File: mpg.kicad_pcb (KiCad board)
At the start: 2 copper layers, 57 parts, among them J1 Conn_01x04_Male, J2 DB25_Male_MountingHoles, J3 Conn_01x03_Male, J4 Screw_Terminal_01x02, J5 Screw_Terminal_01x03, J6 Screw_Terminal_01x03, K1 G5LE-1, Q1 BC847, Q2 BC847, Q3 BC847, Q4 BC847, Q5 BC847, SW1 SW_Push, U1 LD2981ABU33TR, U2 SP3485CN

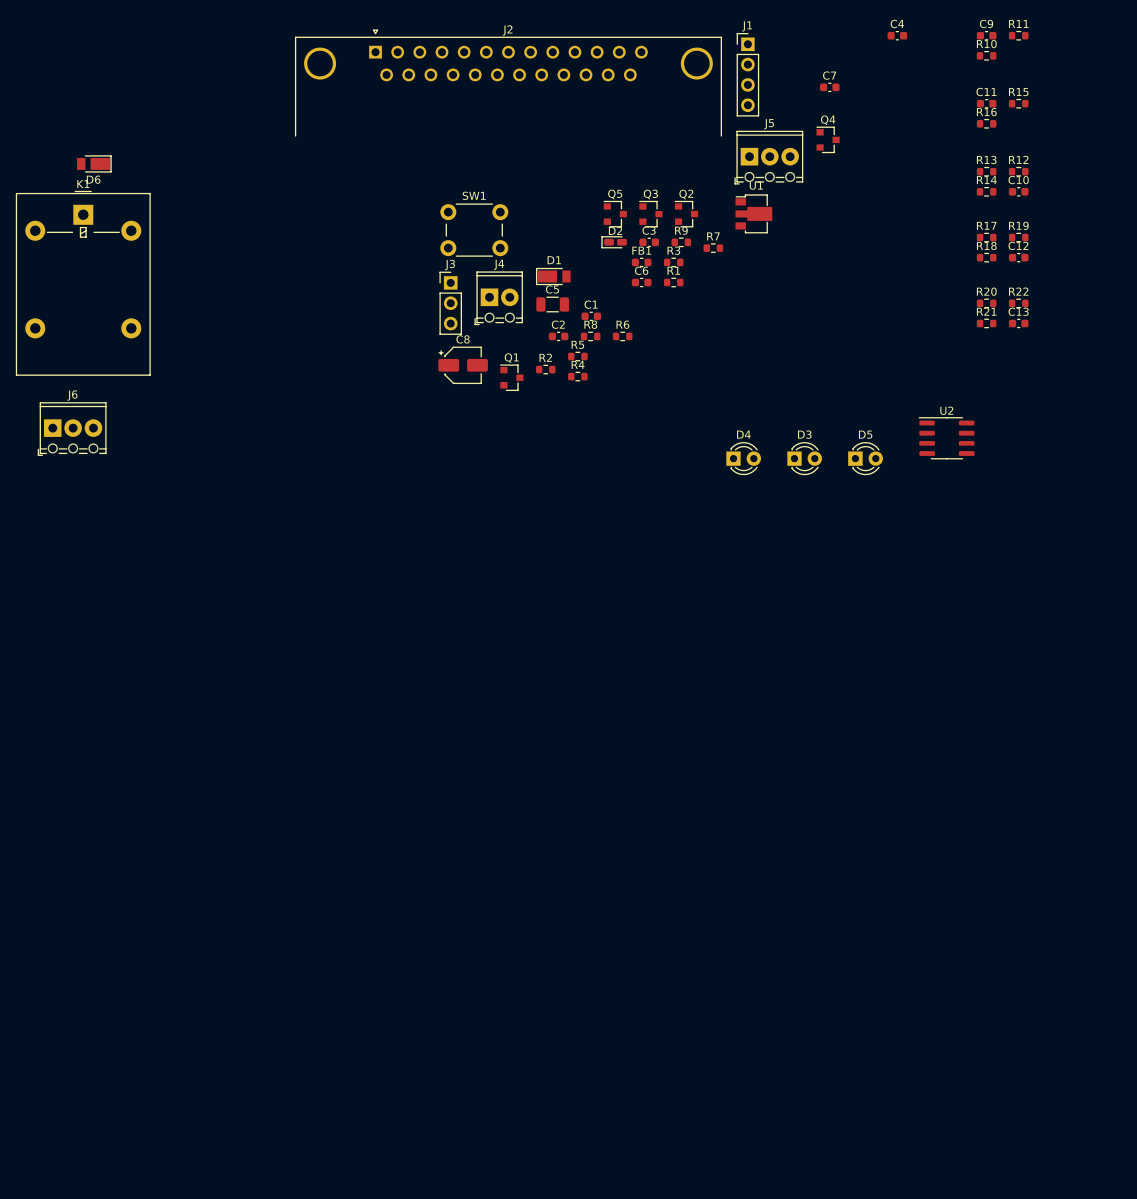
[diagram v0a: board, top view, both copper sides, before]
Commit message: Corrected STM32 symbol and generated PCB.
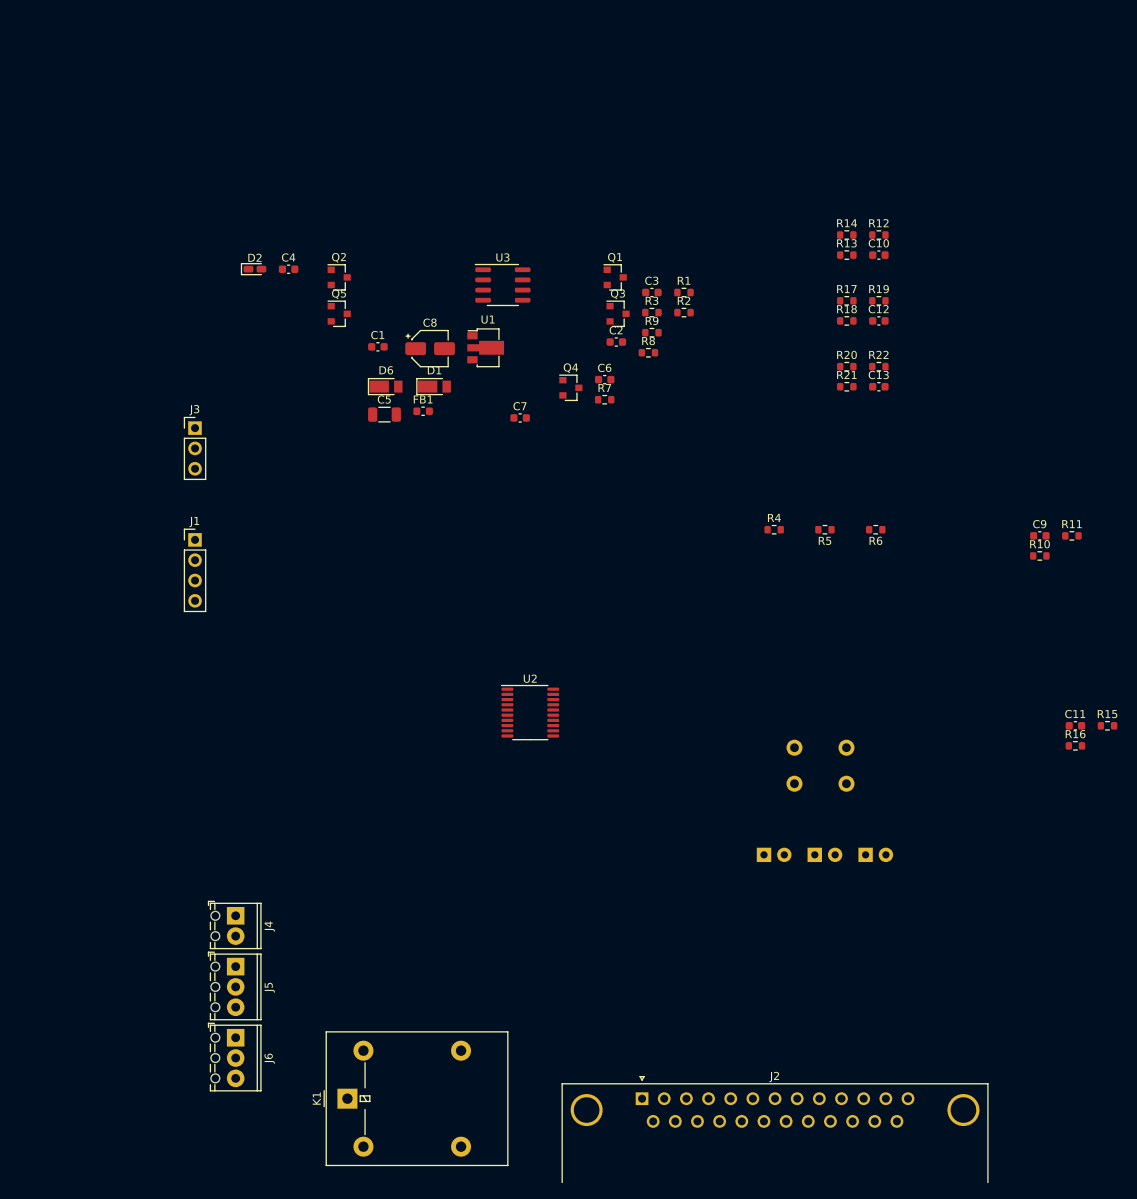
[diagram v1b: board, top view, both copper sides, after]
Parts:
- added U3: SP3485CN, Package_SO:SOIC-8_3.9x4.9mm_P1.27mm, F.Cu at (109.6, 54.5)
- D3, D4, D5, SW1: moved to B.Cu
- U2: value SP3485CN -> STM32G031F4Px; footprint Package_SO:SOIC-8_3.9x4.9mm_P1.27mm -> Package_SO:TSSOP-20_4.4x6.5mm_P0.65mm
- moved J2 135.0 mm to (127.0, 156.2)
- moved J5 119.9 mm to (76.2, 139.7), turned to 270 degrees
- moved K1 115.3 mm to (90.2, 156.2), turned to 90 degrees
- moved J1 92.8 mm to (71.1, 86.4)
- moved J4 83.6 mm to (76.2, 133.3), turned to 270 degrees
- moved SW1 83.5 mm to (146.1, 116.8)
- moved C4 81.5 mm to (82.8, 52.5)
- moved J6 79.6 mm to (76.2, 148.6), turned to 270 degrees
- moved C11 78.5 mm to (181.2, 109.6)
- moved R15 78.5 mm to (185.2, 109.6)
- moved R16 78.5 mm to (181.2, 112.1)
- moved R10 62.9 mm to (176.7, 88.4)
- moved C9 62.9 mm to (176.7, 85.9)
- moved R11 62.9 mm to (180.7, 85.9)
- moved U2 62.3 mm to (113.0, 108.0)
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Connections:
- U2 pad 2: USART1_RTS -> LED_A
- U2 pad 3: USART1_RTS -> LED_B
- U2 pad 4: USART1_TX -> +3V3
- U2 pad 6: Net-(J5-Pad2) -> RESET
- U2 pad 7: Net-(J5-Pad3) -> XYZ
- U2 pad 8: +3V3 -> LED_C

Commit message: Better layout.
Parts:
- moved C4 111.8 mm to (124.0, 156.5)
- moved R3 102.7 mm to (123.4, 160.5)
- moved J1 97.4 mm to (139.2, 156.0), turned to 270 degrees
- moved U3 93.7 mm to (117.9, 147.8), turned to 180 degrees
- moved R22 90.3 mm to (153.4, 154.9)
- moved C13 88.0 mm to (149.4, 154.9)
- moved R2 87.3 mm to (87.9, 133.1)
- moved R20 86.7 mm to (149.4, 151.4)
- moved Q5 85.7 mm to (105.7, 142.2)
- moved Q1 85.4 mm to (153.4, 133.6)
- moved R8 85.4 mm to (111.8, 146.8), turned to 90 degrees
- moved D2 84.8 mm to (87.8, 136.8)
- moved R21 84.2 mm to (153.4, 151.4), turned to 180 degrees
- moved R9 83.7 mm to (110.2, 142.2), turned to 180 degrees
- moved R1 79.0 mm to (149.4, 132.6), turned to 180 degrees
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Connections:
- J2 pad 10: /sheet603130A5/S2 -> XYZ
- J2 pad 11: /sheet603130A5/S3 -> /sheet603130A5/S2
- J2 pad 12: ABC -> /Sheet602C38D3/S2
- J2 pad 13: /Sheet602C38D3/S2 -> ABC
- J2 pad 9: XYZ -> /sheet603130A5/S3
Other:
- board outline added: 97.5 x 59.4 mm

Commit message: Smaller is better!
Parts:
- moved D6 47.6 mm to (138.2, 160.5)
- moved J3 45.2 mm to (153.9, 111.8), turned to 270 degrees
- moved D1 42.4 mm to (112.8, 112.3)
- moved J4 39.8 mm to (110.7, 121.9)
- moved C1 39.7 mm to (134.1, 131.6), turned to 90 degrees
- moved J6 36.3 mm to (110.7, 137.4)
- moved J5 34.8 mm to (110.7, 128.5)
- moved FB1 32.0 mm to (121.4, 121.4), turned to 90 degrees
- moved R7 31.6 mm to (133.1, 144.8), turned to 0 degrees
- moved SW1 31.5 mm to (143.8, 155.4), turned to 90 degrees
- moved D2 30.9 mm to (118.5, 133.4), turned to 180 degrees
- moved R2 30.7 mm to (118.4, 137.2)
- moved C5 29.5 mm to (117.9, 121.4), turned to 180 degrees
- moved K1 29.5 mm to (131.6, 155.4)
- moved C3 29.3 mm to (123.4, 131.6), turned to 90 degrees
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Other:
- board size 97.5 x 59.4 mm -> 63.5 x 59.4 mm

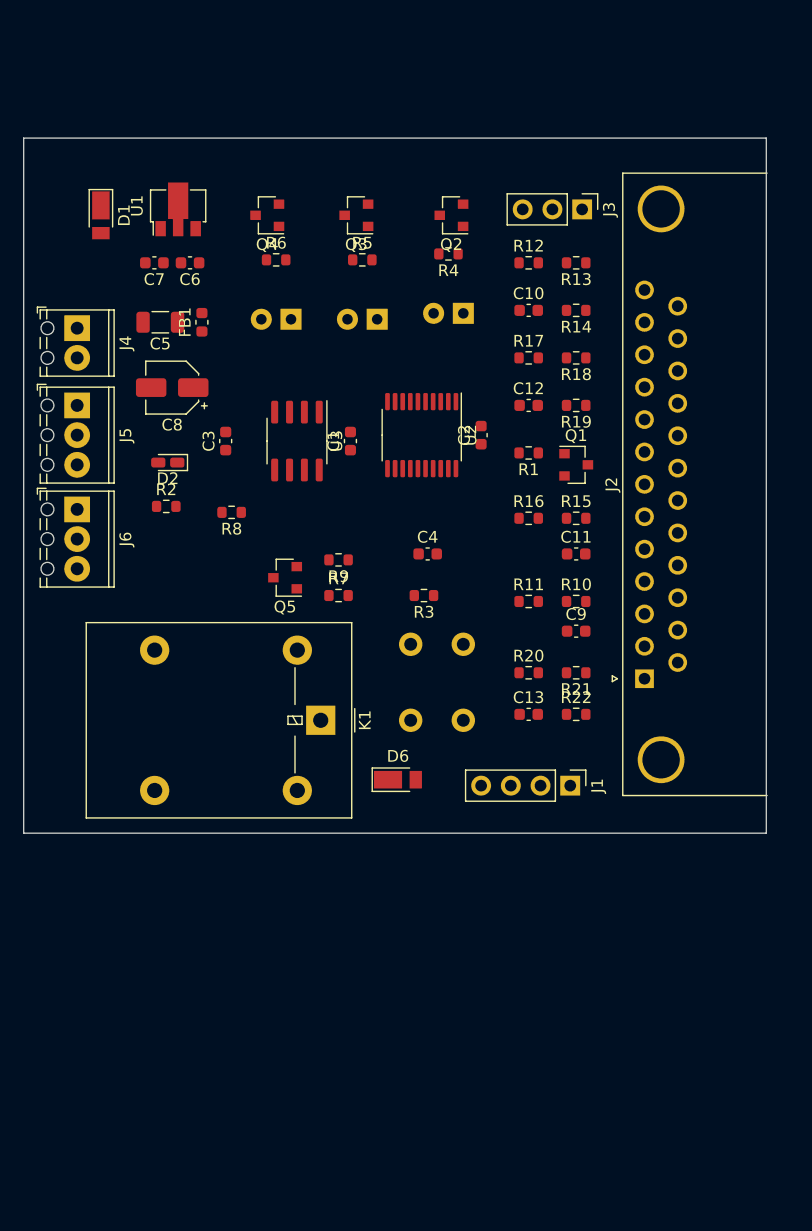
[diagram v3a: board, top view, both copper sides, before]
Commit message: Use RJ45 connector.
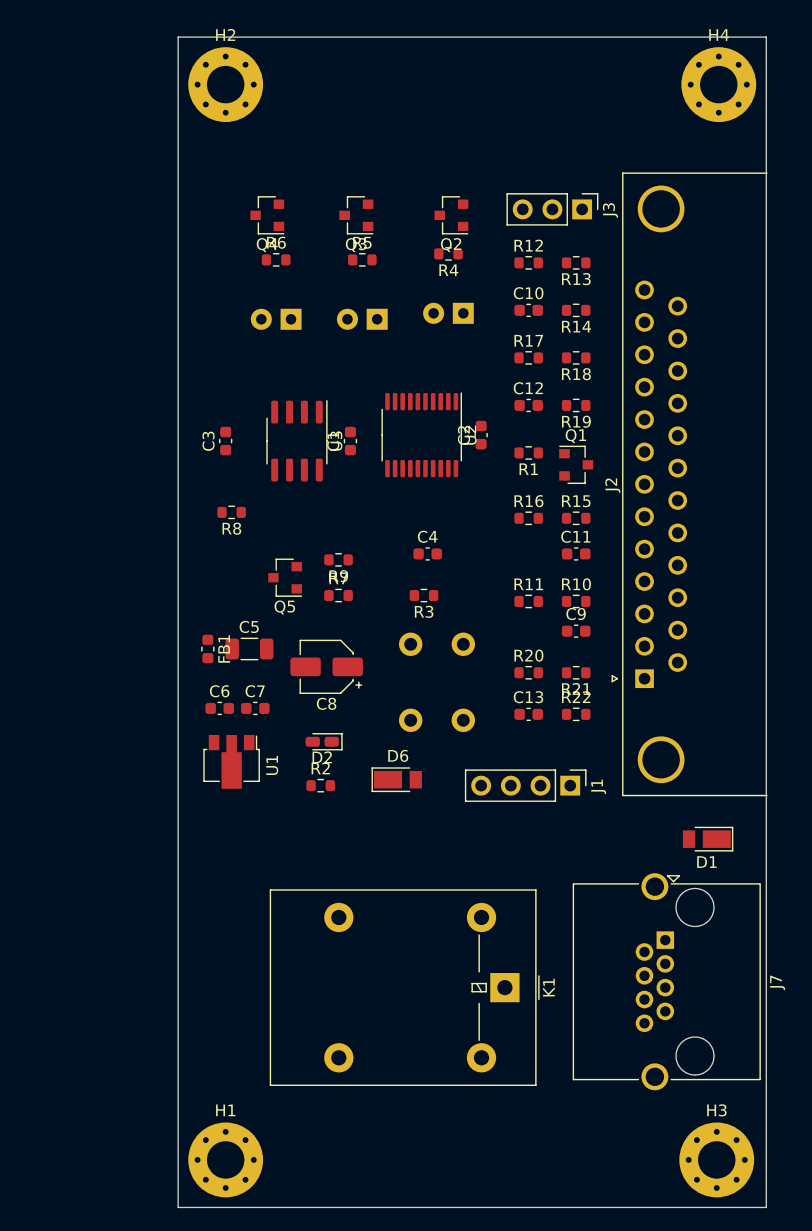
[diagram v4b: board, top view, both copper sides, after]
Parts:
- removed J4: Screw_Terminal_01x02, TerminalBlock_Phoenix:TerminalBlock_Phoenix_MPT-0,5-2-2.54_1x02_P2.54mm_Horizontal
- removed J5, J6: Screw_Terminal_01x03, TerminalBlock_Phoenix:TerminalBlock_Phoenix_MPT-0,5-3-2.54_1x03_P2.54mm_Horizontal
- added H1: MountingHole_Pad, MountingHole:MountingHole_3.2mm_M3_Pad_Via, F.Cu at (123.4, 193.0)
- added H2: MountingHole_Pad, MountingHole:MountingHole_3.2mm_M3_Pad_Via, F.Cu at (123.4, 101.1)
- added H3: MountingHole_Pad, MountingHole:MountingHole_3.2mm_M3_Pad_Via, F.Cu at (165.4, 193.0)
- added H4: MountingHole_Pad, MountingHole:MountingHole_3.2mm_M3_Pad_Via, F.Cu at (165.6, 101.1)
- added J7: RJ45_Shielded, Connector_RJ:RJ45_Amphenol_RJHSE5380, F.Cu at (161.0, 174.2)
- moved D1 74.4 mm to (164.6, 165.6), turned to 180 degrees
- moved U1 47.5 mm to (124.0, 159.0), turned to 270 degrees
- moved C7 39.1 mm to (126.0, 154.4), turned to 0 degrees
- moved C6 38.2 mm to (122.9, 154.4), turned to 0 degrees
- moved C5 29.0 mm to (125.5, 149.4), turned to 0 degrees
- moved FB1 27.9 mm to (121.9, 149.4), turned to 270 degrees
- moved K1 27.8 mm to (147.3, 178.3)
- moved C8 27.3 mm to (132.1, 150.9)
- moved D2 27.3 mm to (131.7, 157.3)
- moved R2 27.3 mm to (131.6, 161.0)
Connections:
- net Net-(J5-Pad2) renamed A
- net Net-(J5-Pad3) renamed B
- D1 pad 2: Net-(D1-Pad2) -> POW
- K1 pad 1: Net-(J6-Pad1) -> GND
- K1 pad 3: Net-(J6-Pad2) -> NO
- K1 pad 4: Net-(J6-Pad3) -> NC
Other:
- board size 63.5 x 59.4 mm -> 50.3 x 100.1 mm
